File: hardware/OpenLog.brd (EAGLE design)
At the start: 17.8 x 19.1 mm, 21 parts, among them Q1 16MHZ, U1 ATMEGA328P_TQFP, U2 3.3V MIC5205, U3 microSD Socket

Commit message: Changed c10 to c4
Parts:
- renumbered C10 to C4
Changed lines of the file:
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@@
 <setting verticaltext="up"/>
 </settings>
-<grid distance="0.05" unitdist="inch" unit="inch" style="lines" multiple="1" display="yes" altdistance="0.0001" altunitdist="inch" altunit="inch"/>
+<grid distance="0.05" unitdist="inch" unit="inch" style="lines" multiple="1" display="yes" altdistance="0.005" altunitdist="inch" altunit="inch"/>
 <layers>
 <layer number="1" name="Top" color="4" fill="1" visible="yes" active="yes"/>
@@
 <layer number="23" name="tOrigins" color="15" fill="1" visible="yes" active="yes"/>
 <layer number="24" name="bOrigins" color="15" fill="1" visible="yes" active="yes"/>
-<layer number="25" name="tNames" color="7" fill="1" visible="no" active="yes"/>
+<layer number="25" name="tNames" color="7" fill="1" visible="yes" active="yes"/>
 <layer number="26" name="bNames" color="7" fill="1" visible="no" active="yes"/>
 <layer number="27" name="tValues" color="7" fill="1" visible="no" active="yes"/>
@@
 </autorouter>
 <elements>
-<element name="C10" library="SparkFun-Capacitors" package="0603-CAP" value="0.1uF" x="34.94278125" y="-2.776215625" smashed="yes" rot="R180">
+<element name="C4" library="SparkFun-Capacitors" package="0603-CAP" value="0.1uF" x="34.94278125" y="-2.776215625" smashed="yes" rot="R180">
 <attribute name="NAME" x="35.83178125" y="-3.474715625" size="0.4064" layer="25" rot="R180"/>
 <attribute name="VALUE" value="0.1uF" x="35.66668125" y="-1.836415625" size="0.4064" layer="27" rot="R180"/>
@@
 <signals>
 <signal name="GND" class="1">
-<contactref element="C10" pad="2"/>
+<contactref element="C4" pad="2"/>
 <contactref element="C3" pad="1"/>
 <contactref element="D3" pad="C"/>
@@
 <signal name="3.3V">
 <contactref element="U2" pad="5"/>
-<contactref element="C10" pad="1"/>
+<contactref element="C4" pad="1"/>
 <contactref element="C1" pad="1"/>
 <contactref element="R2" pad="2"/>

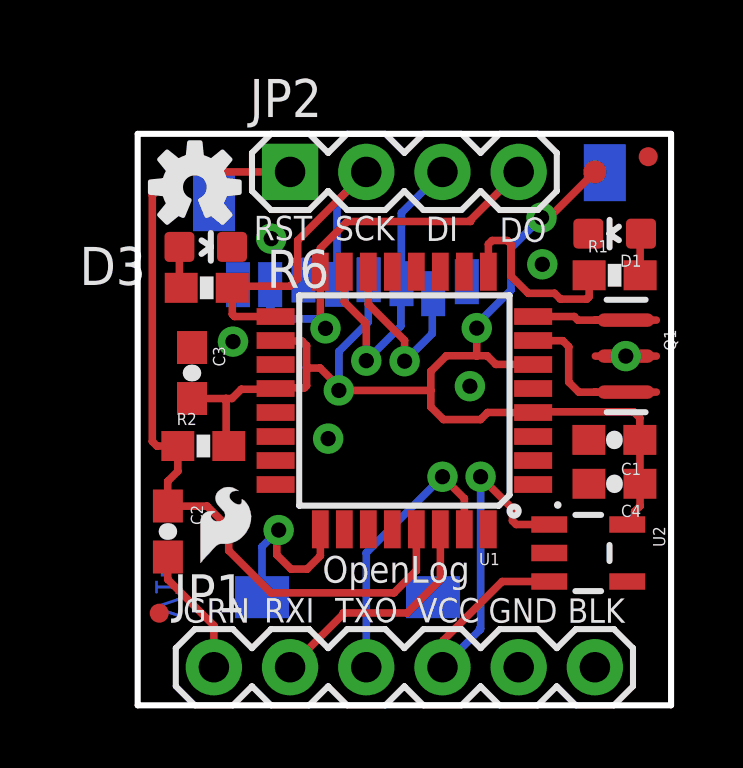
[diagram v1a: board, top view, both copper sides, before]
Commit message: Adding fiducials to bottom side
Adding fiducials to bottom side for SD card socket placement.
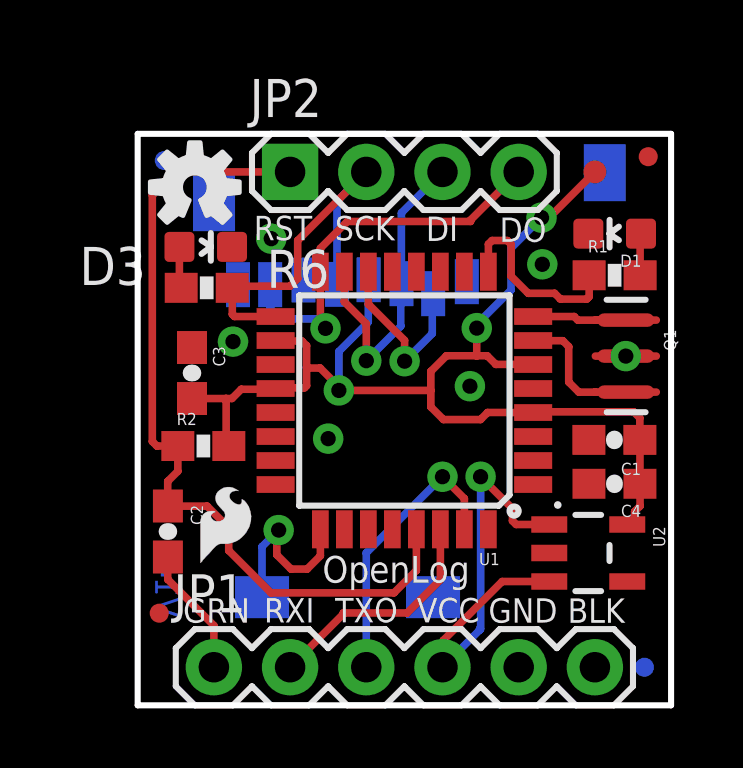
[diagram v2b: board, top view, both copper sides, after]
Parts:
- added FID3, FID4: FIDUCIALUFIDUCIAL, SparkFun-Aesthetics:MICRO-FIDUCIAL
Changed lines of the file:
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@@
 <layer number="23" name="tOrigins" color="15" fill="1" visible="yes" active="yes"/>
 <layer number="24" name="bOrigins" color="15" fill="1" visible="yes" active="yes"/>
-<layer number="25" name="tNames" color="7" fill="1" visible="yes" active="yes"/>
+<layer number="25" name="tNames" color="7" fill="1" visible="no" active="yes"/>
 <layer number="26" name="bNames" color="7" fill="1" visible="no" active="yes"/>
 <layer number="27" name="tValues" color="7" fill="1" visible="no" active="yes"/>
@@
 <layer number="47" name="Measures" color="7" fill="1" visible="no" active="yes"/>
 <layer number="48" name="Document" color="7" fill="1" visible="no" active="yes"/>
-<layer number="49" name="Reference" color="7" fill="1" visible="no" active="yes"/>
+<layer number="49" name="Reference" color="7" fill="1" visible="yes" active="yes"/>
 <layer number="50" name="dxf" color="7" fill="1" visible="no" active="yes"/>
 <layer number="51" name="tDocu" color="6" fill="1" visible="yes" active="yes"/>
@@
 <element name="TP1" library="SparkFun-Passives" package="PAD.03X.03" value="TEST-POINT3" x="34.29" y="7.62"/>
 <element name="LOGO2" library="SparkFun-Aesthetics" package="OSHW-LOGO-S" value="OSHW-LOGOS" x="20.955" y="7.112"/>
+<element name="FID3" library="SparkFun-Aesthetics" package="MICRO-FIDUCIAL" value="FIDUCIALUFIDUCIAL" x="35.941" y="-8.89" rot="MR0"/>
+<element name="FID4" library="SparkFun-Aesthetics" package="MICRO-FIDUCIAL" value="FIDUCIALUFIDUCIAL" x="19.939" y="8.001" rot="MR0"/>
 </elements>
 <signals>
